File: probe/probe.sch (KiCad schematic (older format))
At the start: 27 parts

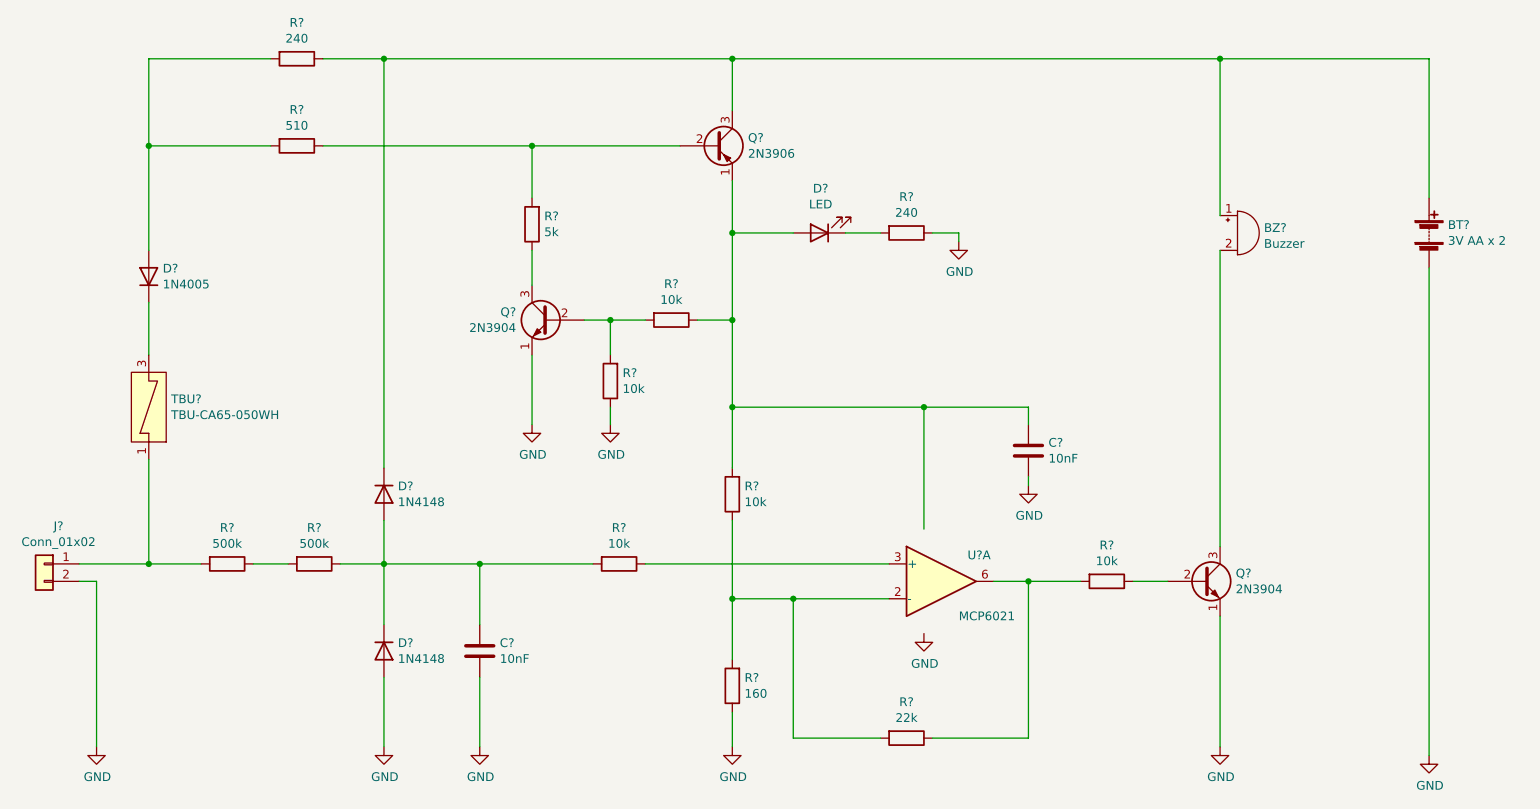
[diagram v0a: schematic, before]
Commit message: Moved library and completed PCB
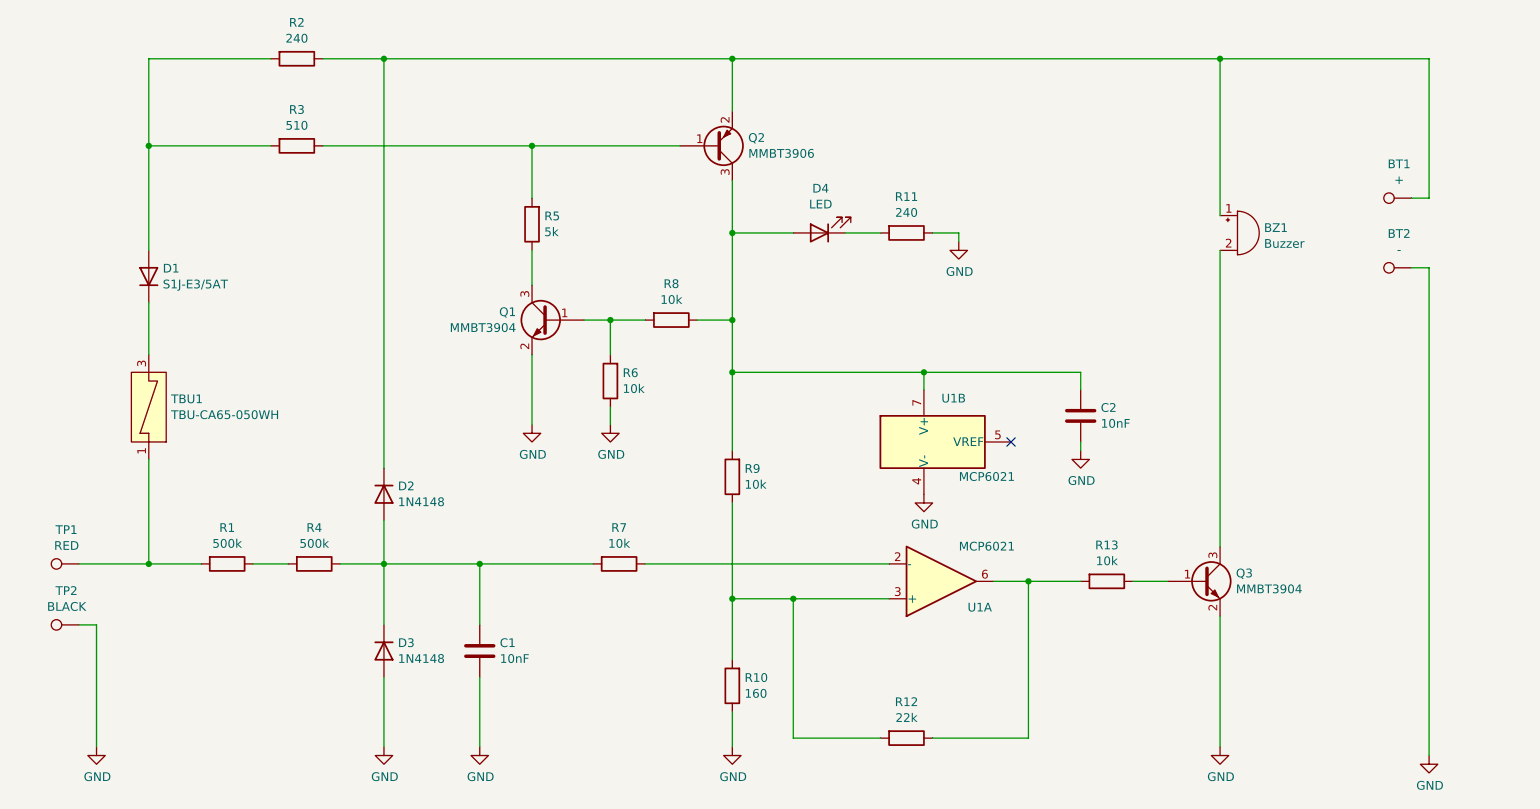
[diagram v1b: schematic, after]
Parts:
- removed BT?: 3V AA x 2, symbol Device:Battery
- removed D?: 1N4148, Diode_THT:D_DO-35_SOD27_P7.62mm_Horizontal, symbol Diode:1N4148
- removed D?: 1N4005, Diode_THT:D_DO-41_SOD81_P10.16mm_Horizontal, symbol Diode:1N4005
- removed J?: Conn_01x02, symbol Connector_Generic:Conn_01x02
- removed Q?: 2N3906, Package_TO_SOT_THT:TO-92_Inline, symbol Transistor_BJT:2N3906
- removed Q? (x2): 2N3904, Package_TO_SOT_THT:TO-92_Inline, symbol Transistor_BJT:2N3904
- added BT1: +, TestPoint:TestPoint_Pad_4.0x4.0mm, symbol Connector:TestPoint
- added BT2: -, TestPoint:TestPoint_Pad_4.0x4.0mm, symbol Connector:TestPoint
- added D1: S1J-E3/5AT, Diode_SMD:D_SMA_Handsoldering, symbol Device:D
- added D3: 1N4148, Diode_SMD:D_SOD-123, symbol Diode:1N4148
- added Q1, Q3: MMBT3904, Package_TO_SOT_SMD:SOT-23_Handsoldering, symbol Transistor_BJT:MMBT3904
- added Q2: MMBT3906, Package_TO_SOT_SMD:SOT-23_Handsoldering, symbol Transistor_BJT:MMBT3906
- added TP1: RED, TestPoint:TestPoint_Pad_4.0x4.0mm, symbol Connector:TestPoint
- added TP2: BLACK, TestPoint:TestPoint_Pad_4.0x4.0mm, symbol Connector:TestPoint
- added unit 2 of U1
- BZ1: renamed from BZ?; footprint (none) -> Buzzer_Beeper:Buzzer_12x9.5RM7.6
- C1, C2: renamed from C?; footprint (none) -> Capacitor_SMD:C_0805_2012Metric_Pad1.18x1.45mm_HandSolder
- D2: renamed from D?; footprint Diode_THT:D_DO-35_SOD27_P7.62mm_Horizontal -> Diode_SMD:D_SOD-123; mouser (none) -> 512-1N4148WS
- D4: renamed from D?; footprint (none) -> LED_THT:LED_D5.0mm
- R1, R10, R12, R13, R2, R3, R4, R5, R6, R7, R8, R9: renamed from R?; footprint (none) -> Resistor_SMD:R_1206_3216Metric_Pad1.30x1.75mm_HandSolder
- R11: renamed from R?; footprint (none) -> Resistor_SMD:R_0805_2012Metric_Pad1.20x1.40mm_HandSolder
- TBU1: renamed from TBU?; footprint (none) -> TBU:TBU-CA; mouser (none) -> 652-TBU-CA050-050-WH
- U1: renamed from U?; footprint Package_TO_SOT_SMD:TSOT-23-5 -> Package_SO:SOIC-8_3.9x4.9mm_P1.27mm
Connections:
- net GND: now also BT2.1, D3.2 (A), Q1.2 (E), Q3.2 (E), TP2.1, U1.4 (V-)
- net at R10.2, R12.2, R9.1: now also U1.3 (+); no longer U1.2 (-)
- net at C2.1, D4.2 (A), R8.1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: now also Q2.3 (C), U1.7 (V+)
- net at R13.1: now also Q3.1 (B)
- net at BZ1.1 (-), D2.1 (K), R2.1: now also BT1.1, Q2.2 (E)
- net at BZ1.2 (+): now also Q3.3 (C)
- net at R6.2, R8.2: now also Q1.1 (B)
- net at R5.1: now also Q1.3 (C)
- net at R3.1, R5.2: now also Q2.1 (B)
- net at R7.1: now also U1.2 (-); no longer U1.3 (+)
- net at C1.1, D2.2 (A), R4.1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: now also D3.1 (K)
- net at R1.2, TBU1.1: now also TP1.1
- net at R2.2, R3.2: now also D1.2 (A)
- net at TBU1.3: now also D1.1 (K)
- no-connect marks 0 -> 1
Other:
- moved on the sheet: C2, R9
